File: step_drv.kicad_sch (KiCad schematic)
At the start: 63 parts, among them J17 X-STEPPER, J18 Y-STEPPER, J19 E0-STEPPER, J20 Z-STEPPER, U6 TMC2226-SA-T, U7 TMC2226-SA-T, U8 TMC2226-SA-T, U9 TMC2226-SA-T

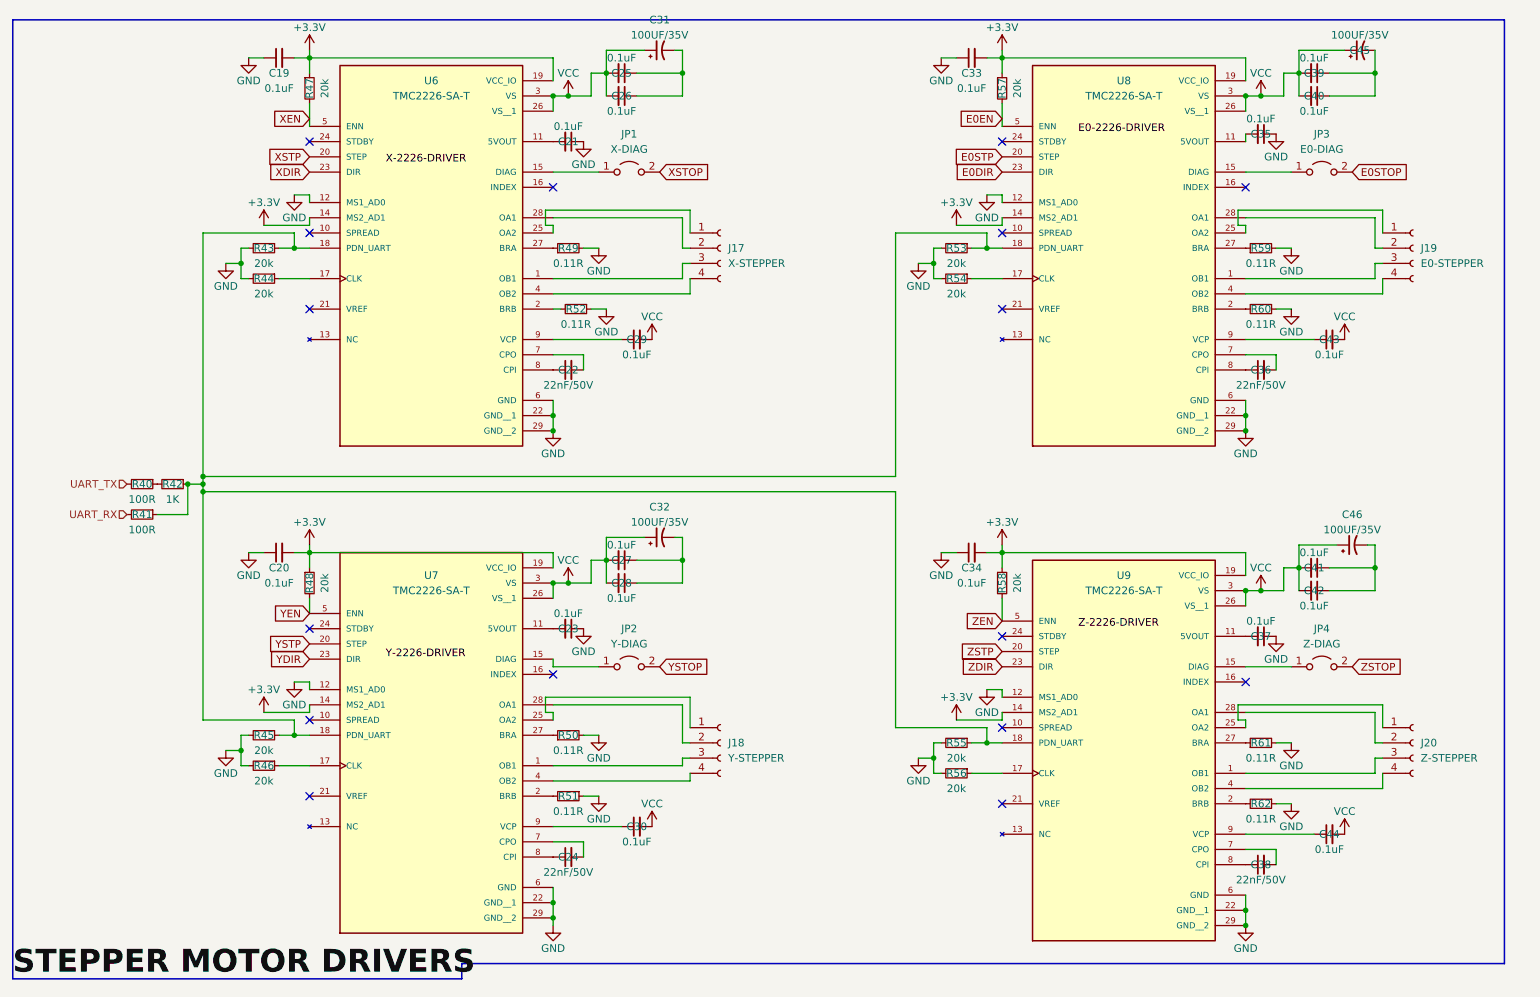
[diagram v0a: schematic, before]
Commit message: Minor Schematic Layout Changes
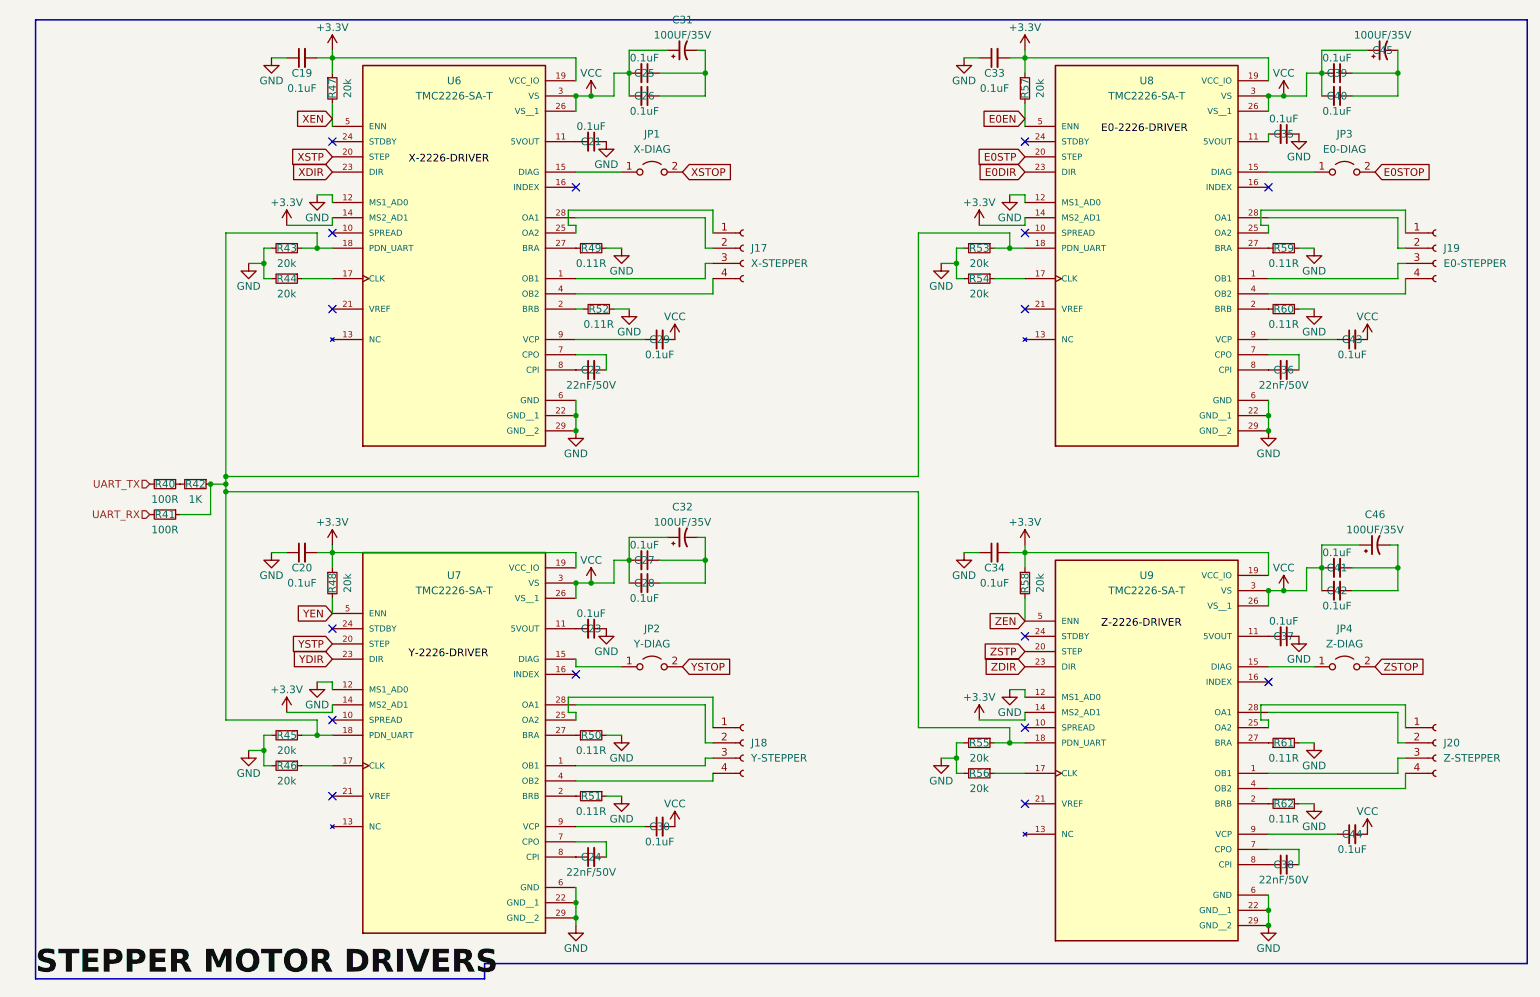
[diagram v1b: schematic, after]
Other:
- moved on the sheet: C19, C20, C21, C22, C23, C24, C25, C26, C27, C28, C29, C30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

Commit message: All components footprinted
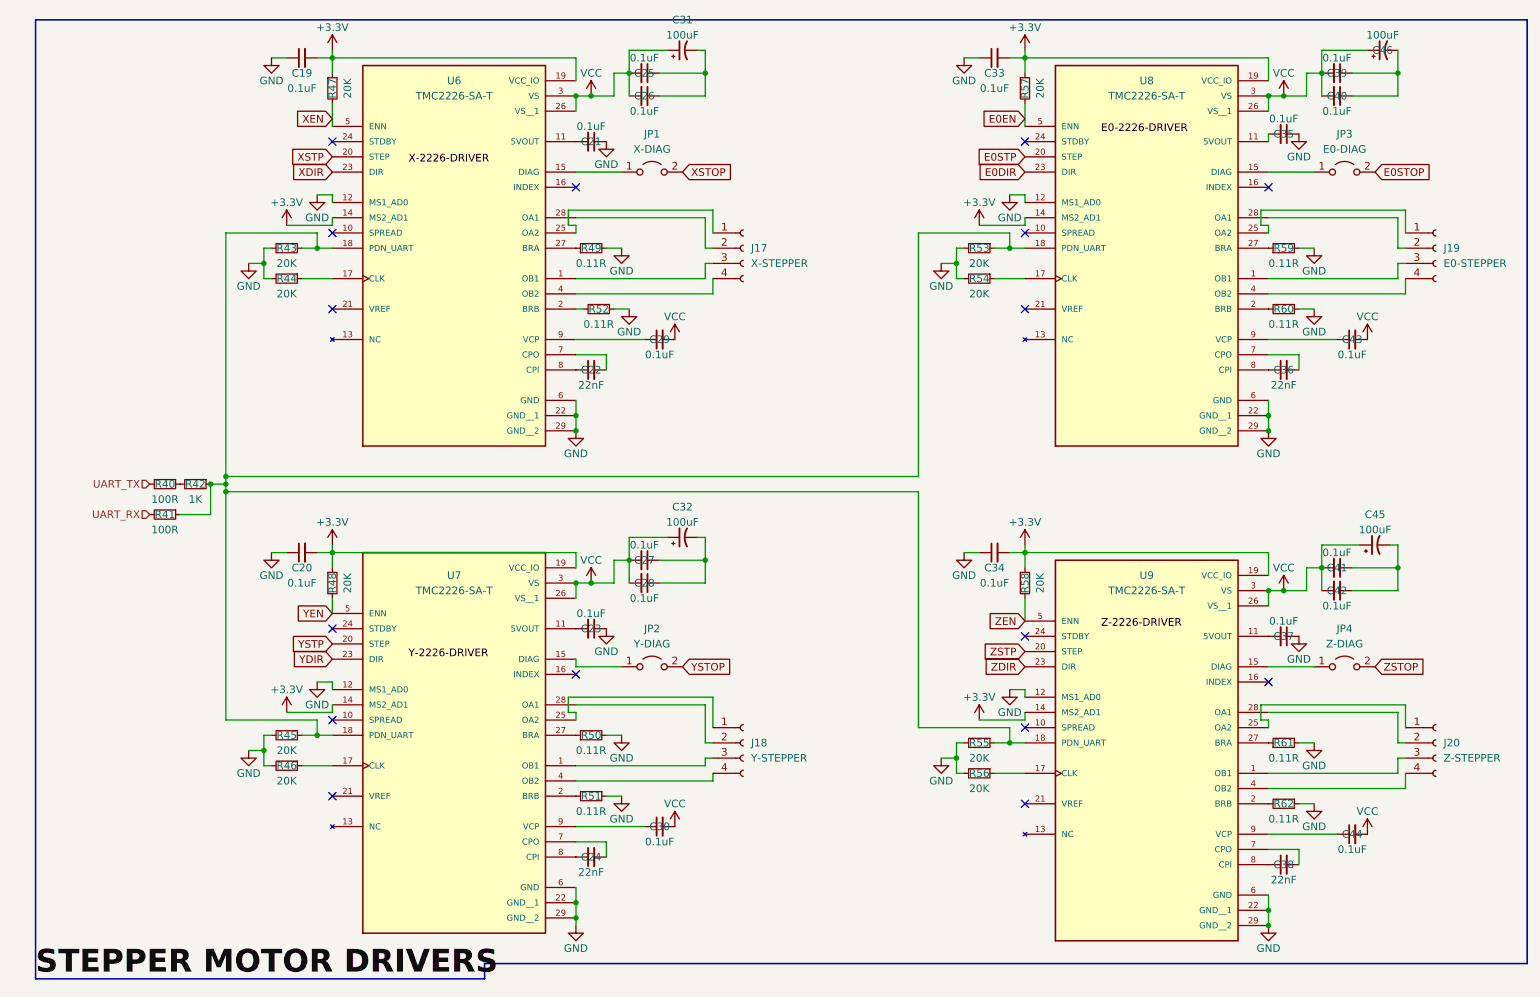
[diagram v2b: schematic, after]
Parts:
- C19, C20, C21, C23, C25, C26, C27, C28, C29, C30, C33, C34, C35, C37, C39, C40, C41, C42, C43, C44: footprint (none) -> Capacitor_SMD:C_1206_3216Metric_Pad1.33x1.80mm_HandSolder
- C22, C24, C36, C38: value 22nF/50V -> 22nF; footprint (none) -> Capacitor_SMD:C_1206_3216Metric_Pad1.33x1.80mm_HandSolder
- C31, C32: value 100UF/35V -> 100uF; footprint (none) -> Capacitor_SMD:C_1206_3216Metric_Pad1.33x1.80mm_HandSolder
- C45: renamed from C46; value 100UF/35V -> 100uF; footprint (none) -> Capacitor_SMD:C_1206_3216Metric_Pad1.33x1.80mm_HandSolder
- C46: renamed from C45; value 100UF/35V -> 100uF; footprint (none) -> Capacitor_SMD:C_1206_3216Metric_Pad1.33x1.80mm_HandSolder
- J17, J18, J19, J20: footprint (none) -> Connector_JST:JST_XH_B3B-XH-A_1x04_P2.50mm_Vertical
- JP1, JP2, JP3, JP4: footprint (none) -> Connector_PinHeader_2.54mm:PinHeader_1x02_P2.54mm_Vertical
- R40, R41, R42, R49, R50, R51, R52, R59, R60, R61, R62: footprint (none) -> Resistor_SMD:R_1206_3216Metric_Pad1.30x1.75mm_HandSolder
- R43, R44, R45, R46, R47, R48, R53, R54, R55, R56, R57, R58: value 20k -> 20K; footprint (none) -> Resistor_SMD:R_1206_3216Metric_Pad1.30x1.75mm_HandSolder
- U6, U7, U8, U9: footprint SOP65P640X120-29N -> TMC2226:SOP65P640X120-29N

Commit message: BOM 99% done
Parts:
- C19, C20, C21, C22, C23, C24, C25, C26, C27, C28, C29, C30, C33, C34, C35, C36, C37, C38, C39, C40, C41, C42, C43, C44: MANUFACTURER (none) -> Samsung
- C31, C32, C45, C46, R40, R41, R42, R43, R44, R45, R46, R47, R48, R49, R50, R51, R52, R53, R54, R55, R56, R57, R58, R59, R60, R61, R62: MANUFACTURER (none) -> Panasonic
- J17, J18, J19, J20: MANUFACTURER (none) -> JST Sales
- JP1, JP2, JP3, JP4: MANUFACTURER (none) -> Molex
- U6, U7, U8, U9: Manufacturer (none) -> Trinamic

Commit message: Totally no 80% re-source of the BOM
suuurely no re-source
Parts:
- added J21: ZB-STEPPER, Connector_JST:JST_XH_B4B-XH-A_1x04_P2.50mm_Vertical, symbol Connector:Conn_01x04_Female
- C19, C20, C21, C22, C23, C24, C25, C26, C27, C28, C29, C30, C33, C34, C35, C36, C37, C38, C39, C40, C41, C42, C43, C44: MANUFACTURER Samsung -> Murata
- C31, C32, C45, C46: footprint Capacitor_SMD:C_1206_3216Metric_Pad1.33x1.80mm_HandSolder -> Capacitor_THT:CP_Radial_D6.3mm_P2.50mm
- J17, J18: footprint Connector_JST:JST_XH_B3B-XH-A_1x04_P2.50mm_Vertical -> Connector_JST:JST_XH_B4B-XH-A_1x04_P2.50mm_Vertical; MANUFACTURER JST Sales -> HCTL
- J19: renamed from J20; value Z-STEPPER -> ZA-STEPPER; footprint Connector_JST:JST_XH_B3B-XH-A_1x04_P2.50mm_Vertical -> Connector_JST:JST_XH_B4B-XH-A_1x04_P2.50mm_Vertical; MANUFACTURER JST Sales -> HCTL
- J20: renamed from J19; footprint Connector_JST:JST_XH_B3B-XH-A_1x04_P2.50mm_Vertical -> Connector_JST:JST_XH_B4B-XH-A_1x04_P2.50mm_Vertical; MANUFACTURER JST Sales -> HCTL
- JP1, JP2, JP3, JP4: MANUFACTURER Molex -> HCTL
- R40, R41: MANUFACTURER Panasonic -> Vishay Intertech
- R42: MANUFACTURER Panasonic -> YAGEO
- R49, R50, R51, R52, R59, R60, R61, R62: footprint Resistor_SMD:R_1206_3216Metric_Pad1.30x1.75mm_HandSolder -> Resistor_SMD:R_2512_6332Metric_Pad1.40x3.35mm_HandSolder; MANUFACTURER Panasonic -> YAGEO
- U6, U7, U8, U9: MAXIMUM_PACKAGE_HEIGHT 1.2mm -> (none); Manufacturer Trinamic -> (none); PARTREV V1.08 -> (none); STANDARD IPC 7351B -> (none)
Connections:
- net at J19.1 (Pin_1), U9.25 (OA2): now also J21.1 (Pin_1)
- net at J19.2 (Pin_2), U9.28 (OA1): now also J21.2 (Pin_2)
- net at J19.3 (Pin_3), U9.1 (OB1): now also J21.3 (Pin_3)
- net at J19.4 (Pin_4), U9.4 (OB2): now also J21.4 (Pin_4)
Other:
- moved on the sheet: J19

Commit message: almost done with layout...
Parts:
- C19, C20, C21, C23, C25, C26, C27, C28, C29, C30, C33, C34, C35, C37, C39, C40, C41, C42, C43, C44: footprint Capacitor_SMD:C_1206_3216Metric_Pad1.33x1.80mm_HandSolder -> Capacitor_SMD:C_0805_2012Metric_Pad1.18x1.45mm_HandSolder; MANUFACTURER Murata -> Samsung Electro Mechanics
- C22, C24, C36, C38: footprint Capacitor_SMD:C_1206_3216Metric_Pad1.33x1.80mm_HandSolder -> Capacitor_SMD:C_0805_2012Metric_Pad1.18x1.45mm_HandSolder; MANUFACTURER Murata -> Taiyo Yuden
- R34: renamed from R40; footprint Resistor_SMD:R_1206_3216Metric_Pad1.30x1.75mm_HandSolder -> Resistor_SMD:R_0805_2012Metric_Pad1.20x1.40mm_HandSolder; MANUFACTURER Vishay Intertech -> YAGEO
- R35: renamed from R41; footprint Resistor_SMD:R_1206_3216Metric_Pad1.30x1.75mm_HandSolder -> Resistor_SMD:R_0805_2012Metric_Pad1.20x1.40mm_HandSolder; MANUFACTURER Vishay Intertech -> YAGEO
- R36: renamed from R42; footprint Resistor_SMD:R_1206_3216Metric_Pad1.30x1.75mm_HandSolder -> Resistor_SMD:R_0805_2012Metric_Pad1.20x1.40mm_HandSolder
- R37: renamed from R43; footprint Resistor_SMD:R_1206_3216Metric_Pad1.30x1.75mm_HandSolder -> Resistor_SMD:R_0805_2012Metric_Pad1.20x1.40mm_HandSolder; MANUFACTURER Panasonic -> YAGEO
- R38: renamed from R44; footprint Resistor_SMD:R_1206_3216Metric_Pad1.30x1.75mm_HandSolder -> Resistor_SMD:R_0805_2012Metric_Pad1.20x1.40mm_HandSolder; MANUFACTURER Panasonic -> YAGEO
- R39: renamed from R45; footprint Resistor_SMD:R_1206_3216Metric_Pad1.30x1.75mm_HandSolder -> Resistor_SMD:R_0805_2012Metric_Pad1.20x1.40mm_HandSolder; MANUFACTURER Panasonic -> YAGEO
- R40: renamed from R46; footprint Resistor_SMD:R_1206_3216Metric_Pad1.30x1.75mm_HandSolder -> Resistor_SMD:R_0805_2012Metric_Pad1.20x1.40mm_HandSolder; MANUFACTURER Panasonic -> YAGEO
- R41: renamed from R47; footprint Resistor_SMD:R_1206_3216Metric_Pad1.30x1.75mm_HandSolder -> Resistor_SMD:R_0805_2012Metric_Pad1.20x1.40mm_HandSolder; MANUFACTURER Panasonic -> YAGEO
- R42: renamed from R48; footprint Resistor_SMD:R_1206_3216Metric_Pad1.30x1.75mm_HandSolder -> Resistor_SMD:R_0805_2012Metric_Pad1.20x1.40mm_HandSolder; MANUFACTURER Panasonic -> YAGEO
- R43: renamed from R49; footprint Resistor_SMD:R_2512_6332Metric_Pad1.40x3.35mm_HandSolder -> Resistor_SMD:R_0805_2012Metric_Pad1.20x1.40mm_HandSolder; MANUFACTURER YAGEO -> Waslin Tech Corp
- R44: renamed from R50; footprint Resistor_SMD:R_2512_6332Metric_Pad1.40x3.35mm_HandSolder -> Resistor_SMD:R_0805_2012Metric_Pad1.20x1.40mm_HandSolder; MANUFACTURER YAGEO -> Waslin Tech Corp
- R45: renamed from R51; footprint Resistor_SMD:R_2512_6332Metric_Pad1.40x3.35mm_HandSolder -> Resistor_SMD:R_0805_2012Metric_Pad1.20x1.40mm_HandSolder; MANUFACTURER YAGEO -> Waslin Tech Corp
- R46: renamed from R52; footprint Resistor_SMD:R_2512_6332Metric_Pad1.40x3.35mm_HandSolder -> Resistor_SMD:R_0805_2012Metric_Pad1.20x1.40mm_HandSolder; MANUFACTURER YAGEO -> Waslin Tech Corp
- R47: renamed from R53; footprint Resistor_SMD:R_1206_3216Metric_Pad1.30x1.75mm_HandSolder -> Resistor_SMD:R_0805_2012Metric_Pad1.20x1.40mm_HandSolder; MANUFACTURER Panasonic -> YAGEO
- R48: renamed from R54; footprint Resistor_SMD:R_1206_3216Metric_Pad1.30x1.75mm_HandSolder -> Resistor_SMD:R_0805_2012Metric_Pad1.20x1.40mm_HandSolder; MANUFACTURER Panasonic -> YAGEO
- R49: renamed from R55; footprint Resistor_SMD:R_1206_3216Metric_Pad1.30x1.75mm_HandSolder -> Resistor_SMD:R_0805_2012Metric_Pad1.20x1.40mm_HandSolder; MANUFACTURER Panasonic -> YAGEO
- R50: renamed from R56; footprint Resistor_SMD:R_1206_3216Metric_Pad1.30x1.75mm_HandSolder -> Resistor_SMD:R_0805_2012Metric_Pad1.20x1.40mm_HandSolder; MANUFACTURER Panasonic -> YAGEO
- R51: renamed from R57; footprint Resistor_SMD:R_1206_3216Metric_Pad1.30x1.75mm_HandSolder -> Resistor_SMD:R_0805_2012Metric_Pad1.20x1.40mm_HandSolder; MANUFACTURER Panasonic -> YAGEO
- R52: renamed from R58; footprint Resistor_SMD:R_1206_3216Metric_Pad1.30x1.75mm_HandSolder -> Resistor_SMD:R_0805_2012Metric_Pad1.20x1.40mm_HandSolder; MANUFACTURER Panasonic -> YAGEO
- R53: renamed from R59; footprint Resistor_SMD:R_2512_6332Metric_Pad1.40x3.35mm_HandSolder -> Resistor_SMD:R_0805_2012Metric_Pad1.20x1.40mm_HandSolder; MANUFACTURER YAGEO -> Waslin Tech Corp
- R54: renamed from R60; footprint Resistor_SMD:R_2512_6332Metric_Pad1.40x3.35mm_HandSolder -> Resistor_SMD:R_0805_2012Metric_Pad1.20x1.40mm_HandSolder; MANUFACTURER YAGEO -> Waslin Tech Corp
- R55: renamed from R61; footprint Resistor_SMD:R_2512_6332Metric_Pad1.40x3.35mm_HandSolder -> Resistor_SMD:R_0805_2012Metric_Pad1.20x1.40mm_HandSolder; MANUFACTURER YAGEO -> Waslin Tech Corp
- R56: renamed from R62; footprint Resistor_SMD:R_2512_6332Metric_Pad1.40x3.35mm_HandSolder -> Resistor_SMD:R_0805_2012Metric_Pad1.20x1.40mm_HandSolder; MANUFACTURER YAGEO -> Waslin Tech Corp
- renumbered C46 to C45, C45 to C46
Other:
- moved on the sheet: C45

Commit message: I am in immense pain
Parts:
- renumbered JP1 to JP2, JP2 to JP3, JP3 to JP4, JP4 to JP5
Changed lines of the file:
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@@
   (symbol (lib_id "Jumper:Jumper_2_Open") (at 233.68 39.37 0) (unit 1)
     (in_bom yes) (on_board yes) (fields_autoplaced)
-    (property "Reference" "JP3" (id 0) (at 233.68 33.02 0))
+    (property "Reference" "JP4" (id 0) (at 233.68 33.02 0))
     (property "Value" "E0-DIAG" (id 1) (at 233.68 35.56 0))
     (property "Footprint" "Connector_PinHeader_2.54mm:PinHeader_1x02_P2.54mm_Vertical" (id 2) (at 233.68 39.37 0)
@@
   (symbol (lib_id "Jumper:Jumper_2_Open") (at 233.68 121.92 0) (unit 1)
     (in_bom yes) (on_board yes) (fields_autoplaced)
-    (property "Reference" "JP4" (id 0) (at 233.68 115.57 0))
+    (property "Reference" "JP5" (id 0) (at 233.68 115.57 0))
     (property "Value" "Z-DIAG" (id 1) (at 233.68 118.11 0))
     (property "Footprint" "Connector_PinHeader_2.54mm:PinHeader_1x02_P2.54mm_Vertical" (id 2) (at 233.68 121.92 0)
@@
   (symbol (lib_id "Jumper:Jumper_2_Open") (at 118.11 39.37 0) (unit 1)
     (in_bom yes) (on_board yes) (fields_autoplaced)
-    (property "Reference" "JP1" (id 0) (at 118.11 33.02 0))
+    (property "Reference" "JP2" (id 0) (at 118.11 33.02 0))
     (property "Value" "X-DIAG" (id 1) (at 118.11 35.56 0))
     (property "Footprint" "Connector_PinHeader_2.54mm:PinHeader_1x02_P2.54mm_Vertical" (id 2) (at 118.11 39.37 0)
@@
   (symbol (lib_id "Jumper:Jumper_2_Open") (at 118.11 121.92 0) (unit 1)
     (in_bom yes) (on_board yes) (fields_autoplaced)
-    (property "Reference" "JP2" (id 0) (at 118.11 115.57 0))
+    (property "Reference" "JP3" (id 0) (at 118.11 115.57 0))
     (property "Value" "Y-DIAG" (id 1) (at 118.11 118.11 0))
     (property "Footprint" "Connector_PinHeader_2.54mm:PinHeader_1x02_P2.54mm_Vertical" (id 2) (at 118.11 121.92 0)
